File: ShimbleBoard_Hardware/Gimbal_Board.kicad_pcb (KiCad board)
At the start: 2 copper layers, 85 parts, among them Q1 Q_NMOS_GDS, Q2 Q_NMOS_GDS, Q3 Q_NMOS_GDS, Q4 Q_NMOS_GDS, Q5 Q_NMOS_GDS, Q6 Q_NMOS_GDS, Q7 Q_NMOS_GDS, Q8 Q_NMOS_GDS, SW1 SW_Push, SW10 SW_SPDT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

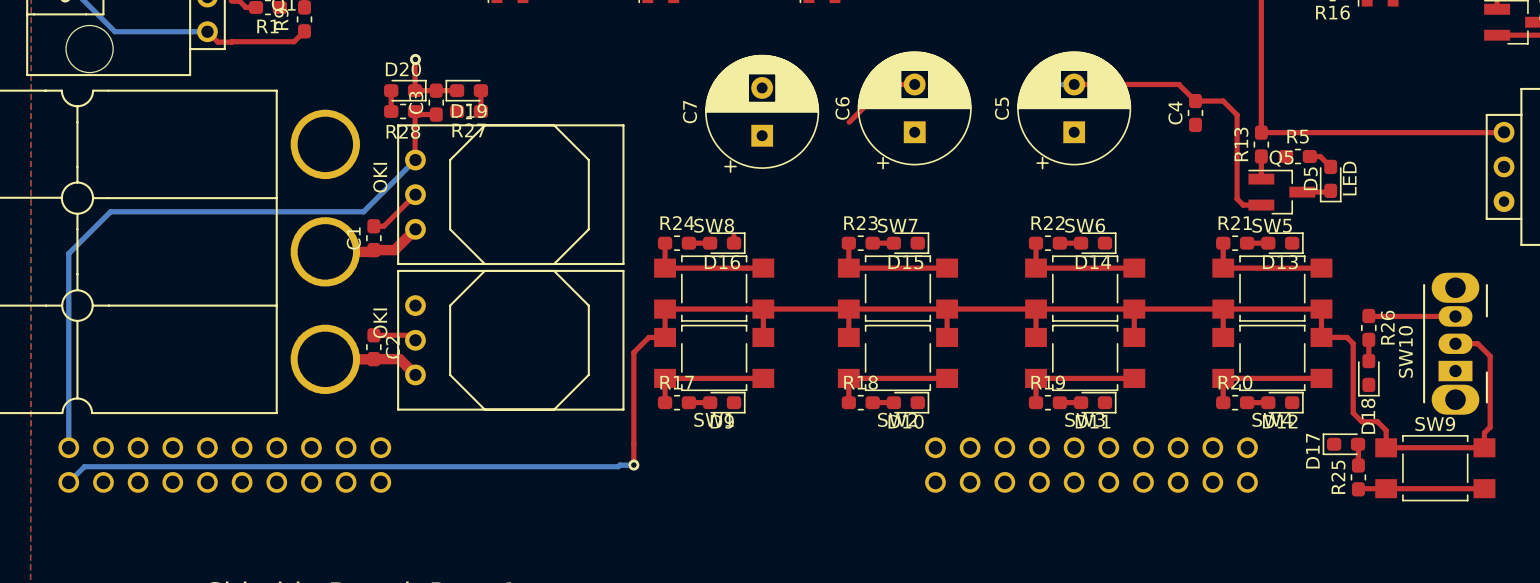
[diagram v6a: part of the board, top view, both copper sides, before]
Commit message: Moved some buttons
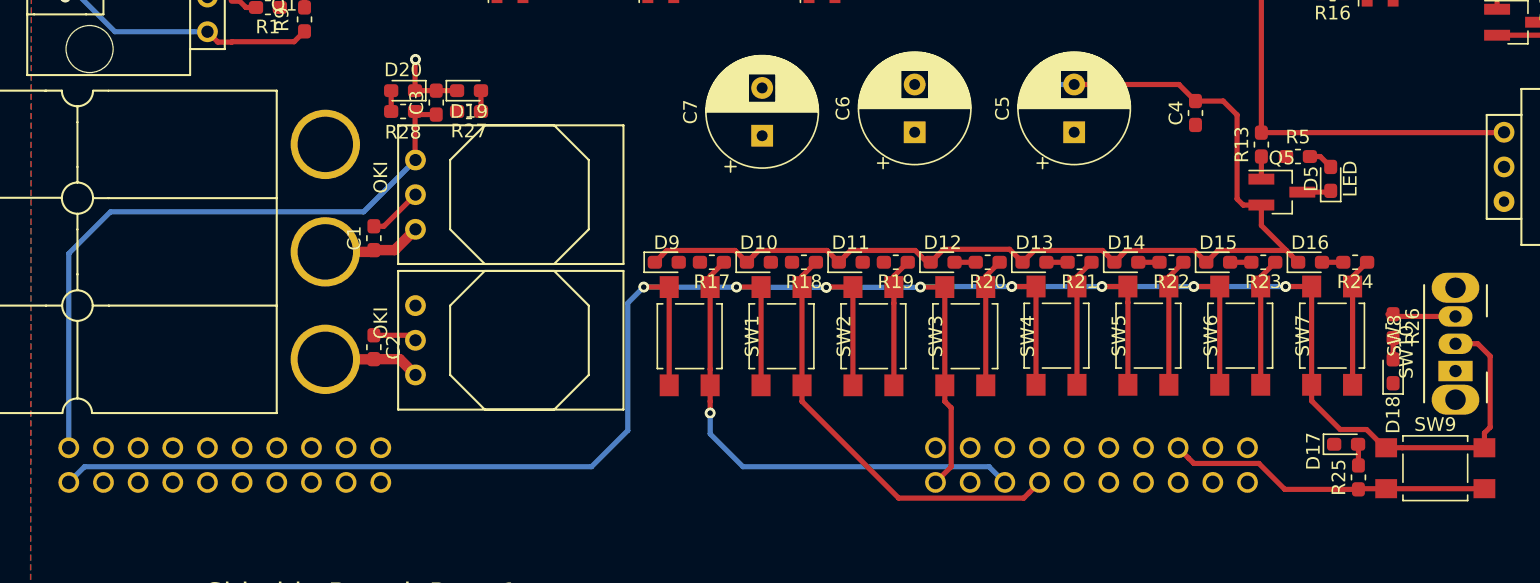
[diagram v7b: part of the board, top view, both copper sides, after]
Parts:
- moved R24 49.7 mm to (162.8, 90.6), turned to 180 degrees
- moved SW8 45.4 mm to (161.1, 95.9), turned to 90 degrees
- moved D16 43.1 mm to (159.5, 90.6), turned to 0 degrees
- moved R23 29.5 mm to (156.1, 90.6), turned to 180 degrees
- moved D12 26.8 mm to (132.6, 90.6), turned to 0 degrees
- moved SW7 25.3 mm to (154.4, 95.9), turned to 90 degrees
- moved D15 22.9 mm to (152.8, 90.6), turned to 0 degrees
- moved SW4 22.6 mm to (134.3, 96.0), turned to 90 degrees
- moved R20 20.8 mm to (135.9, 90.6), turned to 180 degrees
- moved D11 20.5 mm to (125.9, 90.6), turned to 0 degrees
- moved D13 18.1 mm to (139.3, 90.6), turned to 0 degrees
- moved SW5 16.2 mm to (140.9, 95.9), turned to 90 degrees
- moved SW3 15.6 mm to (127.5, 96.0), turned to 90 degrees
- moved R19 15.2 mm to (129.2, 90.6), turned to 180 degrees
- moved D10 14.9 mm to (119.1, 90.6), turned to 0 degrees
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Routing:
- net +3V3: track 147.4 -> 206.6 mm, vias 1 -> 8
- net GND: track 100.5 -> 150.3 mm
- net Servo_SW_1: track 8.98 -> 36.1 mm, vias 0 -> 1
- net Servo_SW_2: track 8.98 -> 31.4 mm
- net Servo_Setup_SW: track 9.25 -> 23.7 mm
- net All_Servo_SW: track 6.36 -> 4.68 mm
- net Net-(D10-Pad2): track 1.55 -> 0.00 mm
- net Net-(D9-Pad2): track 1.55 -> 0.00 mm
- net Net-(D11-Pad2): track 1.55 -> 0.00 mm

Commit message: All Connected I Believe
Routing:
- net All_Servo_SW: track 4.68 -> 48.7 mm, vias 0 -> 2
- net GND: track 150.3 -> 179.1 mm, vias 1 -> 3
- net Servo_SW_3: track 9.44 -> 32.9 mm, vias 0 -> 1
- net Servo_SW_4: track 9.44 -> 28.9 mm, vias 0 -> 1
- net Servo_SW_8: track 9.42 -> 27.1 mm, vias 0 -> 2
- net Servo_SW_5: track 9.42 -> 24.5 mm, vias 0 -> 1
- net Servo_SW_7: track 9.42 -> 24.0 mm
- net Servo_SW_6: track 9.42 -> 20.3 mm, vias 0 -> 1
